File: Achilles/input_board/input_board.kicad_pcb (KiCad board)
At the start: 6 copper layers, 111.8 x 61 mm, 179 parts, among them IC1 LM5157RTER, IC10 ADS8860IDGSR, IC2 TMUX7349FPWR, IC3 TMUX7349FPWR, IC4 TMUX7349FPWR, IC5 TMUX7349FPWR, IC6 MUX509IPW, IC7 MUX509IPW, IC8 MUX36D08IPW, IC9 MUX508IPW, J1 Screw_Terminal_01x02, J10 Programmer, J11 Screw_Terminal_01x02, J2 Screw_Terminal_01x03, J3 Screw_Terminal_01x08, J4 Screw_Terminal_01x08, J5 Screw_Terminal_01x08, J6 Screw_Terminal_01x08, J7 Screw_Terminal_01x02, J8 USB_B, J9 CAN, Q1 CSD19537Q3, Q2 BSS138, U1 TPS26631PWP, U10 INA849DGK, U11 INA849DGK, U12 REF6050xDGK, U13 uA7805, U14 TPS76933, U15 MCP2562, U16 STM32H750ZBTx, U17 TPS565201, U18 INA180A3, U2 TPS7A4701xRGW, U3 INA290A3, U4 INA849DGK, U5 INA849DGK, U6 INA849DGK, U7 INA849DGK, U8 INA849DGK, U9 INA849DGK

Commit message: test version PCB
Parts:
- removed C16, C20, C22, C26, C30, C31, C32, C33: 0.1uF, Capacitor_SMD:C_0805_2012Metric_Pad1.18x1.45mm_HandSolder
- removed C17, C21, C23: 1uF, Capacitor_SMD:C_0805_2012Metric_Pad1.18x1.45mm_HandSolder
- removed IC3, IC4, IC5: TMUX7349FPWR, input_board:SOP65P640X120-20N
- removed J4, J5, J6: Screw_Terminal_01x08, TerminalBlock_Phoenix:TerminalBlock_Phoenix_MPT-0,5-8-2.54_1x08_P2.54mm_Horizontal
- removed R34: 667R, Resistor_SMD:R_0805_2012Metric_Pad1.20x1.40mm_HandSolder
- removed R36: 60.6R, Resistor_SMD:R_0805_2012Metric_Pad1.20x1.40mm_HandSolder
- removed R37: 12R, Resistor_SMD:R_0805_2012Metric_Pad1.20x1.40mm_HandSolder
- removed R38: 6R, Resistor_SMD:R_0805_2012Metric_Pad1.20x1.40mm_HandSolder
- removed U10, U11, U7, U8, U9: INA849DGK, Package_SO:VSSOP-8_3x3mm_P0.65mm
- added TP10: AMP2-, TestPoint:TestPoint_Keystone_5000-5004_Miniature, F.Cu at (71.0, 66.0)
- added TP11: AMP2+, TestPoint:TestPoint_Keystone_5000-5004_Miniature, F.Cu at (75.0, 66.0)
- added TP12: A2_OUT, TestPoint:TestPoint_Keystone_5000-5004_Miniature, F.Cu at (80.0, 79.0)
- added TP13: AMP3-, TestPoint:TestPoint_Keystone_5000-5004_Miniature, F.Cu at (79.0, 66.0)
- added TP14: AMP3+, TestPoint:TestPoint_Keystone_5000-5004_Miniature, F.Cu at (83.0, 66.0)
- added TP15: A3_OUT, TestPoint:TestPoint_Keystone_5000-5004_Miniature, F.Cu at (85.0, 79.0)
- added TP16: REF_OUT, TestPoint:TestPoint_Keystone_5000-5004_Miniature, F.Cu at (90.5, 60.2)
- added TP17: CAL, TestPoint:TestPoint_Keystone_5000-5004_Miniature, F.Cu at (86.8, 61.2)
- added TP18: AINP, TestPoint:TestPoint_Keystone_5000-5004_Miniature, F.Cu at (87.5, 70.8)
- added TP19: IN_A0, TestPoint:TestPoint_Keystone_5000-5004_Miniature, F.Cu at (59.8, 57.5)
- added TP20: IN_A1, TestPoint:TestPoint_Keystone_5000-5004_Miniature, F.Cu at (63.2, 57.5)
- added TP21: SF_1..4, TestPoint:TestPoint_Keystone_5000-5004_Miniature, F.Cu at (86.9, 99.8)
- added TP22: FF_1..4, TestPoint:TestPoint_Keystone_5000-5004_Miniature, F.Cu at (90.8, 99.8)
- added TP23: EN, TestPoint:TestPoint_Keystone_5000-5004_Miniature, F.Cu at (51.5, 62.2)
- added TP24: AMPS0, TestPoint:TestPoint_Keystone_5000-5004_Miniature, F.Cu at (64.0, 83.8)
- added TP25: AMPS1, TestPoint:TestPoint_Keystone_5000-5004_Miniature, F.Cu at (67.5, 83.8)
- added TP26: AMPS2, TestPoint:TestPoint_Keystone_5000-5004_Miniature, F.Cu at (71.0, 83.8)
- added TP27: AMPIN-, TestPoint:TestPoint_Keystone_5000-5004_Miniature, F.Cu at (55.5, 69.0)
- added TP28: AMPIN-, TestPoint:TestPoint_Keystone_5000-5004_Miniature, F.Cu at (59.0, 69.0)
- added TP29: SEL_IN_2, TestPoint:TestPoint_Keystone_5000-5004_Miniature, F.Cu at (83.0, 99.8)
- added TP30: SEL_IN_3, TestPoint:TestPoint_Keystone_5000-5004_Miniature, F.Cu at (94.8, 99.8)
- added TP7: A1_OUT, TestPoint:TestPoint_Keystone_5000-5004_Miniature, F.Cu at (77.8, 83.0)
- added TP8: AMP1-, TestPoint:TestPoint_Keystone_5000-5004_Miniature, F.Cu at (67.0, 66.0)
- added TP9: AMP1+, TestPoint:TestPoint_Keystone_5000-5004_Miniature, F.Cu at (63.0, 66.0)
- C67: value C -> 1.1nF
- R45, R46: value R_US -> 15R
- RN1: value MAX5490TA05000-T -> MAX5490GA01000-T
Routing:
- net /Frontend/FAULT_9..12: track 68.5 -> 7.22 mm, vias 1 -> 0
- net /Frontend/SF_9..12: track 74.2 -> 20.2 mm, vias 1 -> 0
- net /Frontend/SF_5..8: track 55.6 -> 13.1 mm, vias 1 -> 0
- net /Frontend/INPUT_A1: track 174.9 -> 133.1 mm, vias 6 -> 3
- net /Frontend/FAULT_13..16: track 54.6 -> 15.5 mm, vias 1 -> 0
- net /Frontend/INPUT_A0: track 162.5 -> 125.4 mm, vias 4 -> 2
- net /Frontend/IN_5..8+: track 36.4 -> 0.00 mm, vias 2 -> 0
- net /Frontend/IN_5..8-: track 35.3 -> 0.00 mm, vias 2 -> 0
- net /Amplifiers/AMP4+: track 35.2 -> 0.00 mm, vias 2 -> 0
- net /Frontend/IN_13..16-: track 34.3 -> 0.00 mm, vias 2 -> 0
- net /Frontend/EN_1..4: track 169.5 -> 136.1 mm, vias 11 -> 7
- net /Frontend/FAULT_5..8: track 40.8 -> 8.17 mm, vias 1 -> 0
- net /Frontend/IN_13..16+: track 31.4 -> 0.00 mm, vias 2 -> 0
- net GND: track 127.9 -> 97.8 mm, vias 134 -> 117
- net /Frontend/SF_13..16: track 40.8 -> 11.2 mm, vias 1 -> 0
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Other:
- board text added: "A1+"
- board text added: "A1-"
- board text added: "A1OUT"
- board text added: "A2+"
- board text added: "A2-"
- board text added: "A2OUT"
- board text added: "A3+"
- board text added: "A3-"
- board text added: "A3OUT"
- board text added: "ADC_IN"
- board text added: "AINN"
- board text added: "AINP"
- board text added: "AMPS_0"
- board text added: "AMPS_1"
- board text added: "AMPS_2"
- board text added: "CAL"
- board text added: "EN"
- board text added: "FAULT"
- board text added: "IN_A0"
- board text added: "IN_A1"
- board text added: "REF_OUT"
- board text added: "SEL_IN_2"
- board text added: "SEL_IN_3"
- board text added: "SF"
- board text removed: "IN5+"
- board text removed: "IN5-"
- board text removed: "IN6+"
- board text removed: "IN6-"
- board text removed: "IN7+"
- board text removed: "IN7-"
- board text removed: "IN8+"
- board text removed: "IN8-"

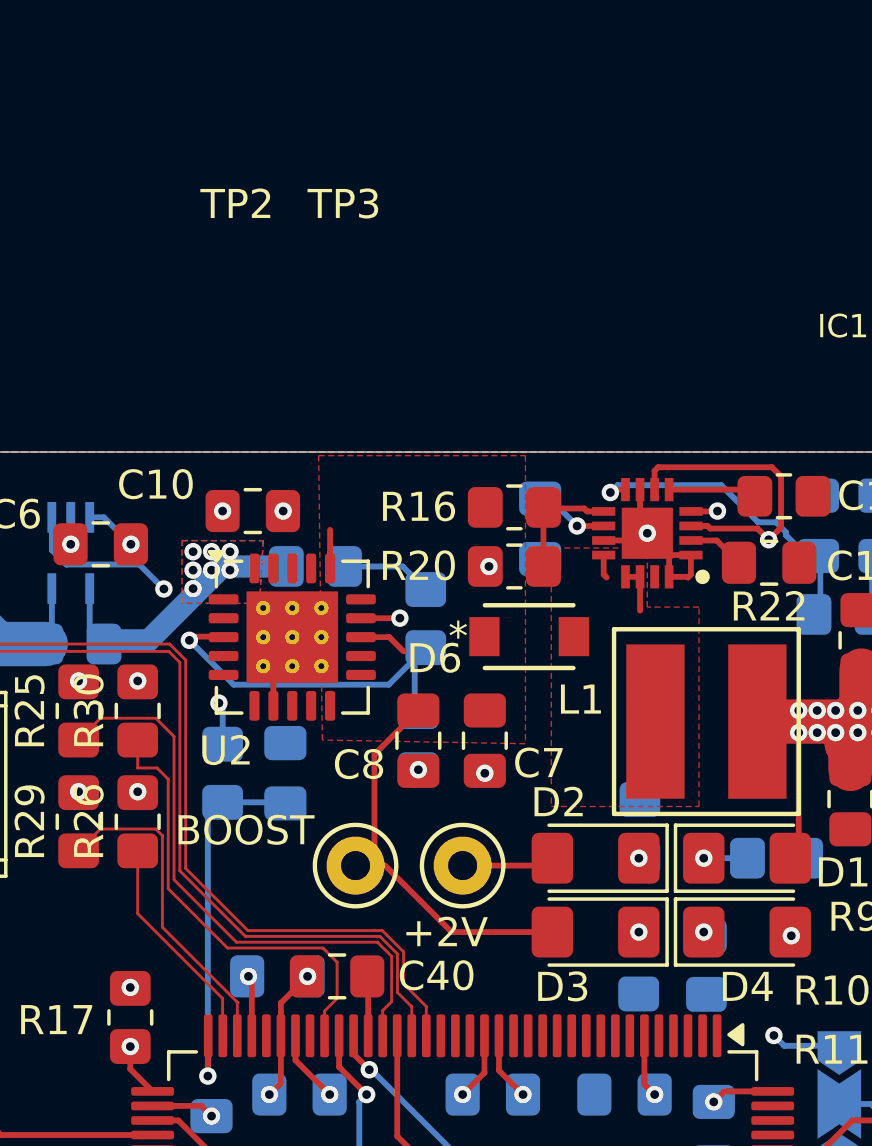
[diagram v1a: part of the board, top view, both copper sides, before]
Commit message: Resize boost caps in sim; update pcb with PNs
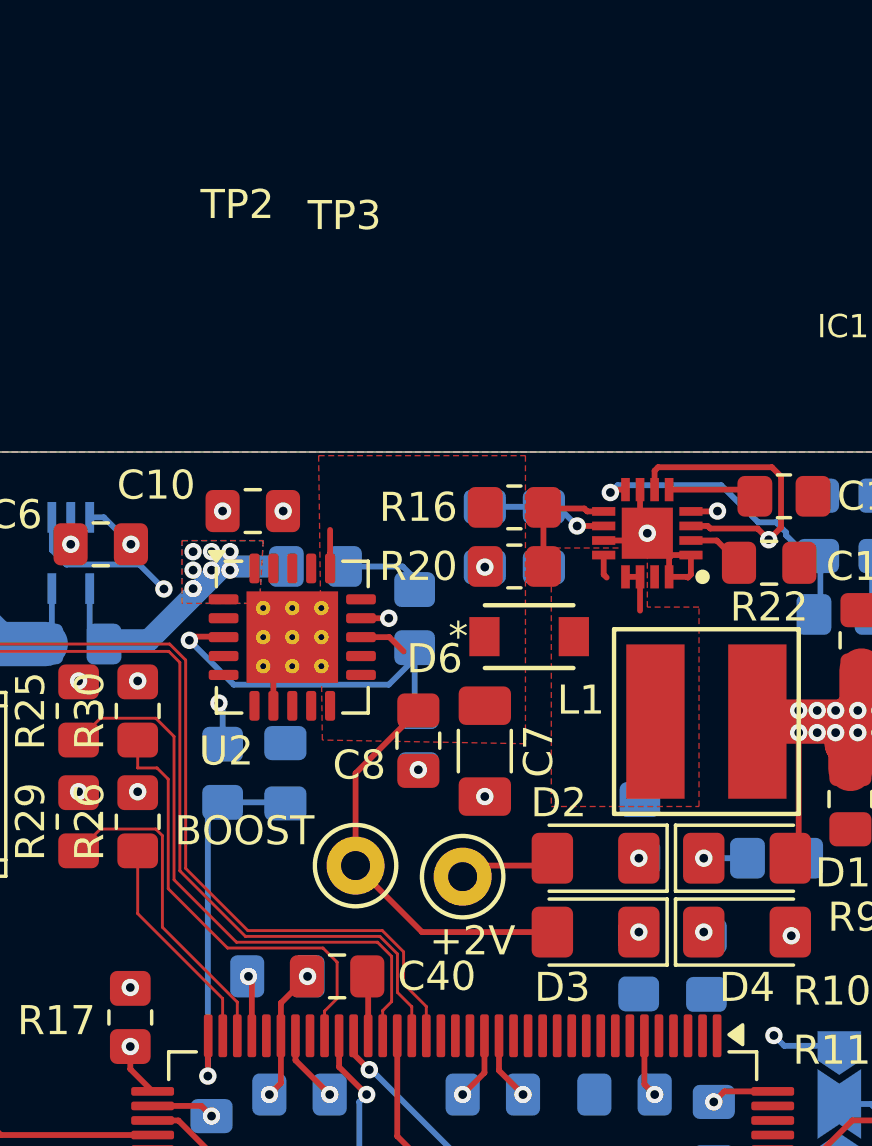
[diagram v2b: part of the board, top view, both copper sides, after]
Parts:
- added C2: 10nF, Capacitor_SMD:C_0805_2012Metric_Pad1.18x1.45mm_HandSolder, B.Cu at (121.4, 48.6)
- C66, C9: value 1.6nF -> 1.6uF
- C7: footprint Capacitor_SMD:C_0805_2012Metric_Pad1.18x1.45mm_HandSolder -> Capacitor_SMD:C_1206_3216Metric_Pad1.33x1.80mm_HandSolder
- moved R15 0.38 mm to (119.0, 51.5)
- moved TP3 0.38 mm to (120.7, 60.3)
- moved C7 0.36 mm to (121.4, 56.0)
- moved C13 0.30 mm to (123.4, 48.6)
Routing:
- net Net-(IC1-SS): track 2.24 -> 4.27 mm
